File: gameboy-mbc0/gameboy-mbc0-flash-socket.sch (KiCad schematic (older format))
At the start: 2 parts, among them P1 CONN_01X32, U1 SST39SF010

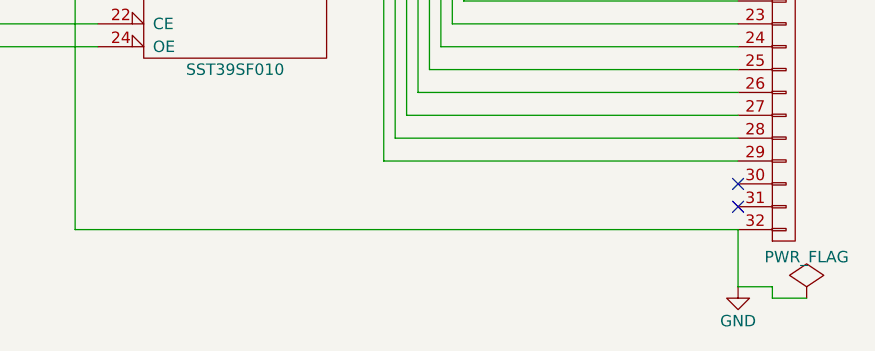
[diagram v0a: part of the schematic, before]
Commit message: added power smoothing capacitors and board outline
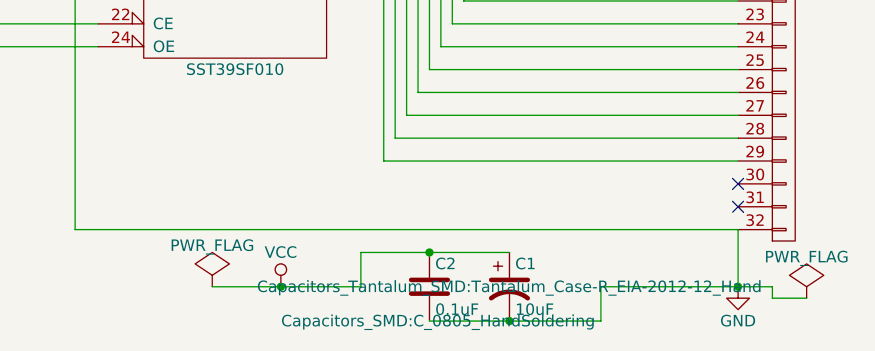
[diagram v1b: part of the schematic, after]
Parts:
- added C1: 10uF, Capacitors_Tantalum_SMD:Tantalum_Case-R_EIA-2012-12_Hand, symbol CP1
- added C2: 0.1uF, Capacitors_SMD:C_0805_HandSoldering, symbol C
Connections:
- net GND: now also C1.2, C2.2
- net VCC: now also C1.1, C2.1
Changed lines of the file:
@@
 	7650 6200 7650 6150
 Wire Wire Line
-	7650 6150 7500 6150
+	7650 6150 6900 6150
+$Comp
+L CP1 C1
+U 1 1 5854355F
+P 6500 6150
+F 0 "C1" H 6525 6250 50  0000 L CNN
+F 1 "10uF" H 6525 6050 50  0000 L CNN
+F 2 "Capacitors_Tantalum_SMD:Tantalum_Case-R_EIA-2012-12_Hand" H 6500 6150 50  0000 C CNN
+F 3 "" H 6500 6150 50  0000 C CNN
+	1    6500 6150
+	1    0    0    -1
+$EndComp
+$Comp
+L C C2
+U 1 1 585435D2
+P 6150 6150
+F 0 "C2" H 6175 6250 50  0000 L CNN
+F 1 "0.1uF" H 6175 6050 50  0000 L CNN
+F 2 "Capacitors_SMD:C_0805_HandSoldering" H 6188 6000 50  0000 C CNN
+F 3 "" H 6150 6150 50  0000 C CNN
+	1    6150 6150
+	1    0    0    -1
+$EndComp
+Wire Wire Line
+	6900 6150 6900 6300
+Wire Wire Line
+	6900 6300 6150 6300
+Connection ~ 7500 6150
+Connection ~ 6500 6300
+$Comp
+L VCC #PWR05
+U 1 1 585437E1
+P 5500 6150
+F 0 "#PWR05" H 5500 6000 50  0001 C CNN
+F 1 "VCC" H 5500 6300 50  0000 C CNN
+F 2 "" H 5500 6150 50  0000 C CNN
+F 3 "" H 5500 6150 50  0000 C CNN
+	1    5500 6150
+	1    0    0    -1
+$EndComp
+$Comp
+L PWR_FLAG #FLG06
+U 1 1 58543829
+P 5200 6150
+F 0 "#FLG06" H 5200 6245 50  0001 C CNN
+F 1 "PWR_FLAG" H 5200 6330 50  0000 C CNN
+F 2 "" H 5200 6150 50  0000 C CNN
+F 3 "" H 5200 6150 50  0000 C CNN
+	1    5200 6150
+	1    0    0    -1
+$EndComp
+Wire Wire Line
+	5200 6150 5850 6150
+Wire Wire Line
+	5850 6150 5850 6000
+Wire Wire Line
+	5850 6000 6500 6000
+Connection ~ 5500 6150
+Connection ~ 6150 6000
 $EndSCHEMATC
